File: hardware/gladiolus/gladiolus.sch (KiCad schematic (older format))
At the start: 133 parts, among them J1 NEIGHBOR1, J2 NEIGHBOR2, J7 BONUS_ROW, P1 CONN_01X05, Q1 Q_NPN_BEC, U1 THS4520RGT, U2 AD8330ARQZ, U3 AD9283, U4 AD9704, U5 LMH6643

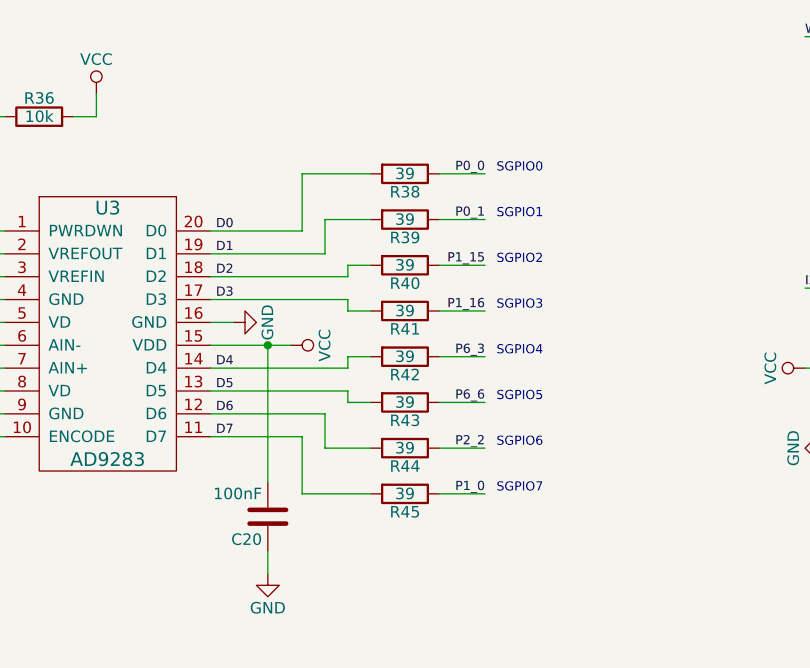
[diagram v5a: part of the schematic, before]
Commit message: Gladiolus: updated series resistor values to match those used at ShmooCon 2017
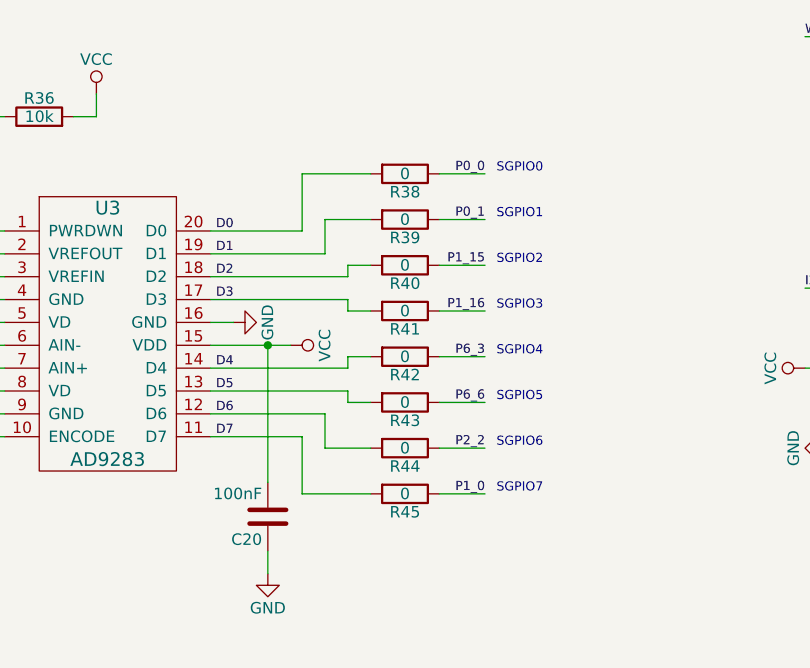
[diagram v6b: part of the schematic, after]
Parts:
- R38, R39, R40, R41, R42, R43, R44, R45: value 39 -> 0; Description RES SMD 39 OHM 5% 1/10W 0603 -> RES SMD 0.0OHM JUMPER 1/10W 0603; Part Number RC0603JR-0739RL -> RC0603JR-070RL

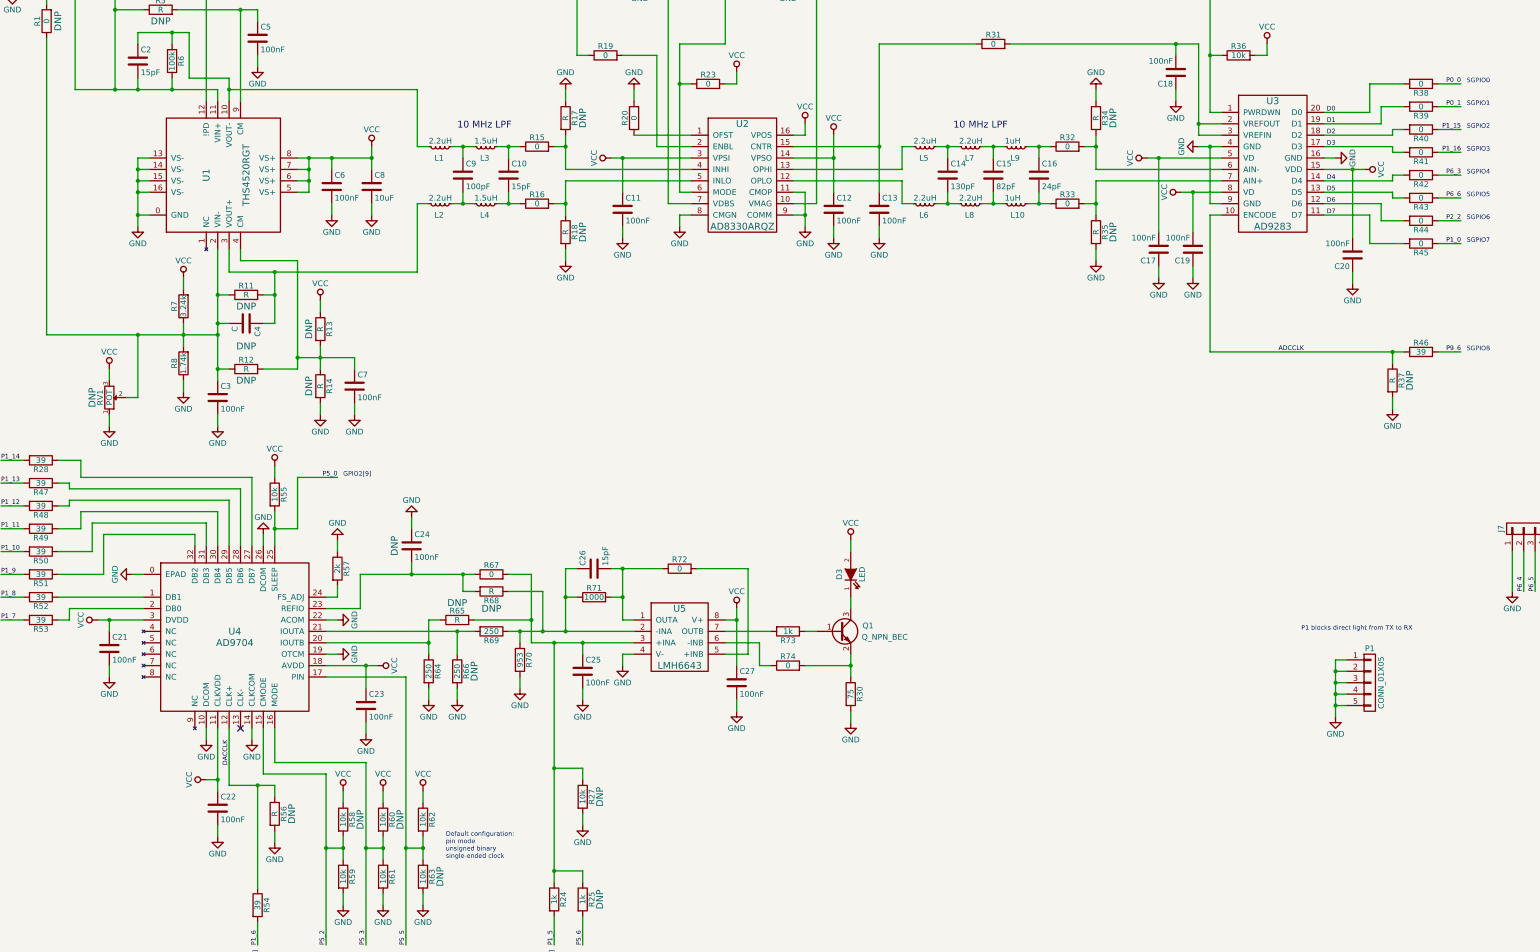
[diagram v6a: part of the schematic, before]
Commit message: Gladiolus: added LED/photodiode expansion to P1
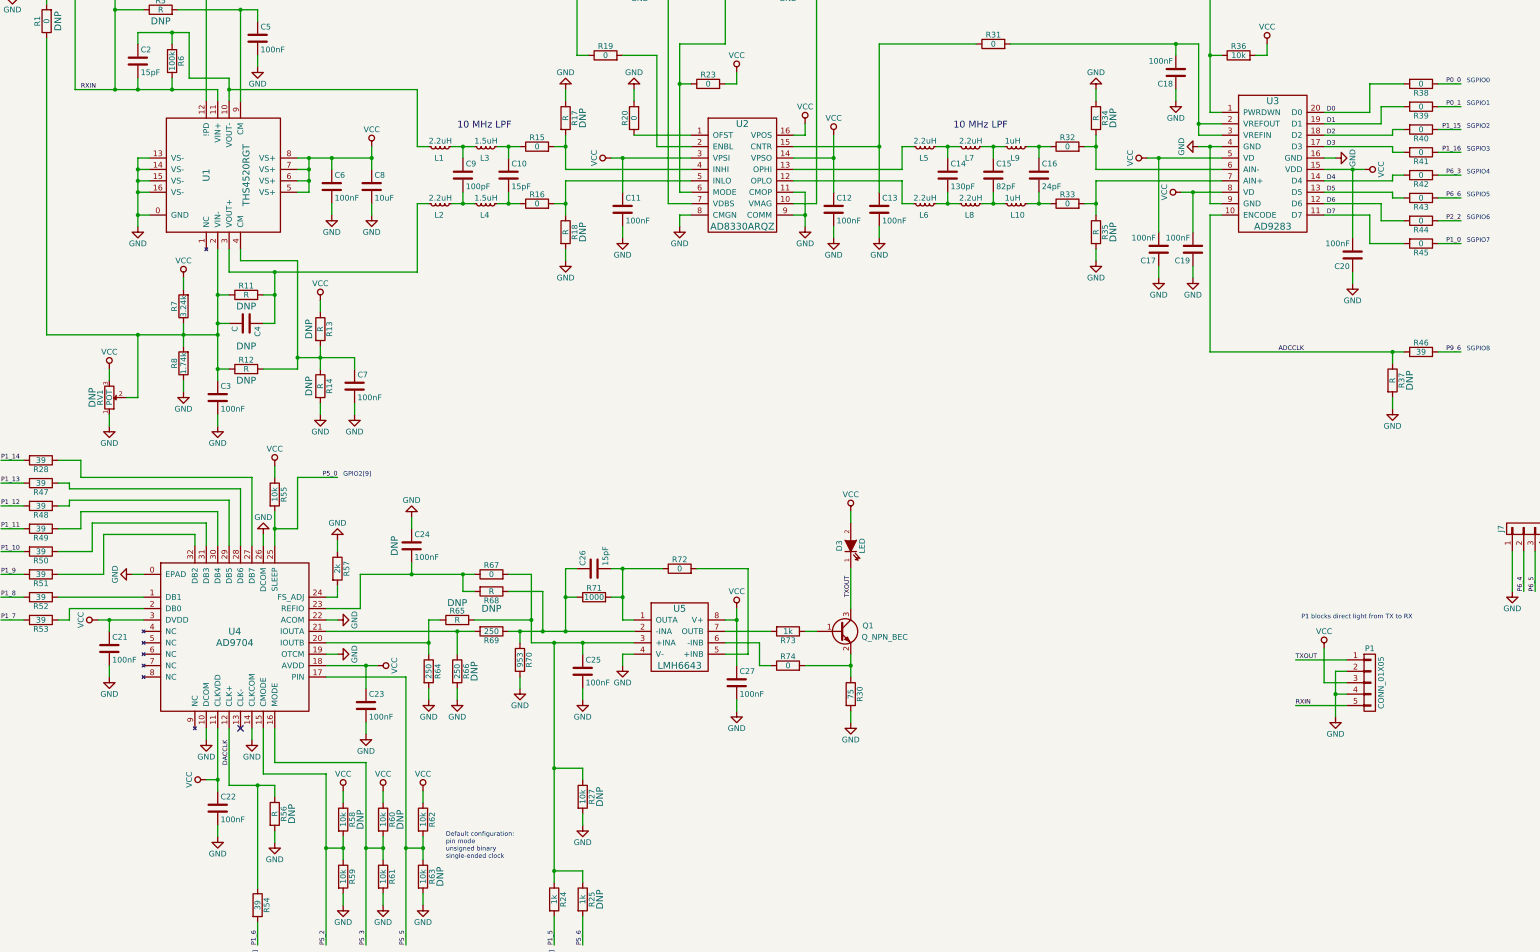
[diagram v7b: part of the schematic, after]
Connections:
- net GND: no longer P1.1 (P1), P1.3 (P3), P1.5 (P5)
- net VCC: now also P1.3 (P3)
- net RXIN: now reaches C2.2, D1.2 (A), D2.2 (A), R5.1, R6.2, U1.11 (VIN+)
- net RXIN: now also P1.5 (P5)
- net TXOUT: now reaches D3.1 (K), Q1.3 (C)
- net TXOUT: now also P1.1 (P1)
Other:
- moved on the sheet: D3
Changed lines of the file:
@@
 L LED D3
 U 1 1 58496E3C
-P 8450 6900
-F 0 "D3" H 8450 7000 50  0000 C CNN
-F 1 "LED" H 8450 6800 50  0000 C CNN
-F 2 "LEDs:LED-5MM" H 8450 6900 50  0001 C CNN
-F 3 "" H 8450 6900 50  0000 C CNN
-F 4 "Vishay" H 8450 6900 60  0001 C CNN "Manufacturer"
-F 5 "TSHF5210" H 8450 6900 60  0001 C CNN "Part Number"
-F 6 "Infrared (IR) Emitter 890nm 1.4V 100mA 120mW/sr @ 100mA 20° Radial, 5mm Dia (T 1 3/4)" H 8450 6900 60  0001 C CNN "Description"
-	1    8450 6900
+P 8450 6650
+F 0 "D3" H 8450 6750 50  0000 C CNN
+F 1 "LED" H 8450 6550 50  0000 C CNN
+F 2 "LEDs:LED-5MM" H 8450 6650 50  0001 C CNN
+F 3 "" H 8450 6650 50  0000 C CNN
+F 4 "Vishay" H 8450 6650 60  0001 C CNN "Manufacturer"
+F 5 "TSHF5210" H 8450 6650 60  0001 C CNN "Part Number"
+F 6 "Infrared (IR) Emitter 890nm 1.4V 100mA 120mW/sr @ 100mA 20° Radial, 5mm Dia (T 1 3/4)" H 8450 6650 60  0001 C CNN "Description"
+	1    8450 6650
 	0    -1   -1   0
 $EndComp
@@
 L VCC #PWR046
 U 1 1 58498676
-P 8450 6600
-F 0 "#PWR046" H 8450 6450 50  0001 C CNN
-F 1 "VCC" H 8450 6750 50  0000 C CNN
-F 2 "" H 8450 6600 60  0000 C CNN
-F 3 "" H 8450 6600 60  0000 C CNN
-	1    8450 6600
+P 8450 6350
+F 0 "#PWR046" H 8450 6200 50  0001 C CNN
+F 1 "VCC" H 8450 6500 50  0000 C CNN
+F 2 "" H 8450 6350 60  0000 C CNN
+F 3 "" H 8450 6350 60  0000 C CNN
+	1    8450 6350
 	1    0    0    -1
 $EndComp
@@
 	1    0    0    -1
 $EndComp
-Text Notes 12400 7400 0    40   ~ 0
+Text Notes 12400 7300 0    40   ~ 0
 P1 blocks direct light from TX to RX
 $Comp
@@
 Wire Wire Line
 	5550 7800 5550 7900
-Connection ~ 12700 8050
-Wire Wire Line
-	12700 8050 12800 8050
-Connection ~ 12700 7950
-Wire Wire Line
-	12700 7950 12800 7950
-Connection ~ 12700 7850
-Wire Wire Line
-	12700 7850 12800 7850
-Connection ~ 12700 7750
-Wire Wire Line
-	12800 7750 12700 7750
-Wire Wire Line
-	12700 7650 12700 8150
-Wire Wire Line
-	12800 7650 12700 7650
+Wire Wire Line
+	12350 8050 12800 8050
+Wire Wire Line
+	12800 7650 12350 7650
 Wire Wire Line
 	11600 3750 11600 4950
@@
 	8050 7400 8150 7400
 Wire Wire Line
-	8450 7100 8450 7200
+	8450 6850 8450 7200
 Wire Wire Line
 	8450 7600 8450 7800
@@
 	8450 8100 8450 8200
 Wire Wire Line
-	8450 6600 8450 6700
+	8450 6350 8450 6450
 Wire Wire Line
 	13000 2600 13300 2600
@@
 	6100 9600 6100 9500
 Wire Wire Line
-	6100 9500 5850 9500
+	5850 9500 6100 9500
 Connection ~ 5850 9500
 $Comp
@@
 Wire Wire Line
 	6600 800  6600 900
+Text Label 1700 2650 0    40   ~ 0
+RXIN
+Text Label 12350 8050 0    40   ~ 0
+RXIN
+Text Label 12350 7650 0    40   ~ 0
+TXOUT
+Text Label 8450 7100 1    40   ~ 0
+TXOUT
+Wire Wire Line
+	12800 7750 12700 7750
+Wire Wire Line
+	12700 7750 12700 8150
+Wire Wire Line
+	12800 7950 12700 7950
+Connection ~ 12700 7950
+$Comp
+L VCC #PWR?
+U 1 1 5883D349
+P 12600 7550
+F 0 "#PWR?" H 12600 7400 50  0001 C CNN
+F 1 "VCC" H 12600 7700 50  0000 C CNN
+F 2 "" H 12600 7550 60  0000 C CNN
+F 3 "" H 12600 7550 60  0000 C CNN
+	1    12600 7550
+	1    0    0    -1
+$EndComp
+Wire Wire Line
+	12800 7850 12600 7850
+Wire Wire Line
+	12600 7850 12600 7550
 $EndSCHEMATC

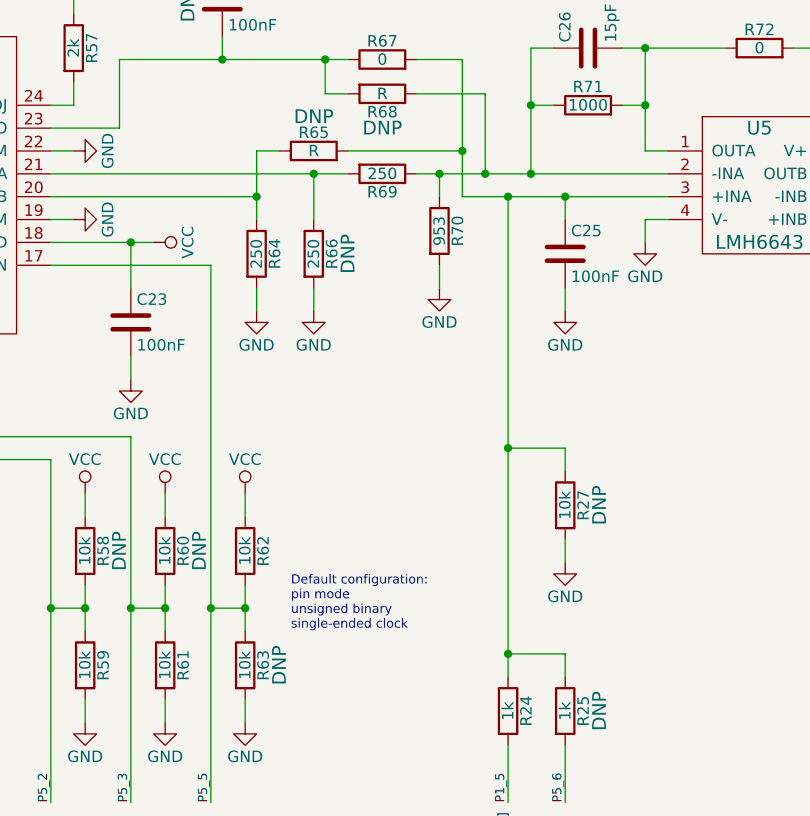
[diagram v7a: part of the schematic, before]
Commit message: Added part numbers for R57, R64, R66, R69, & R71; Changed values of R64, R66, & R69 to reflect part.
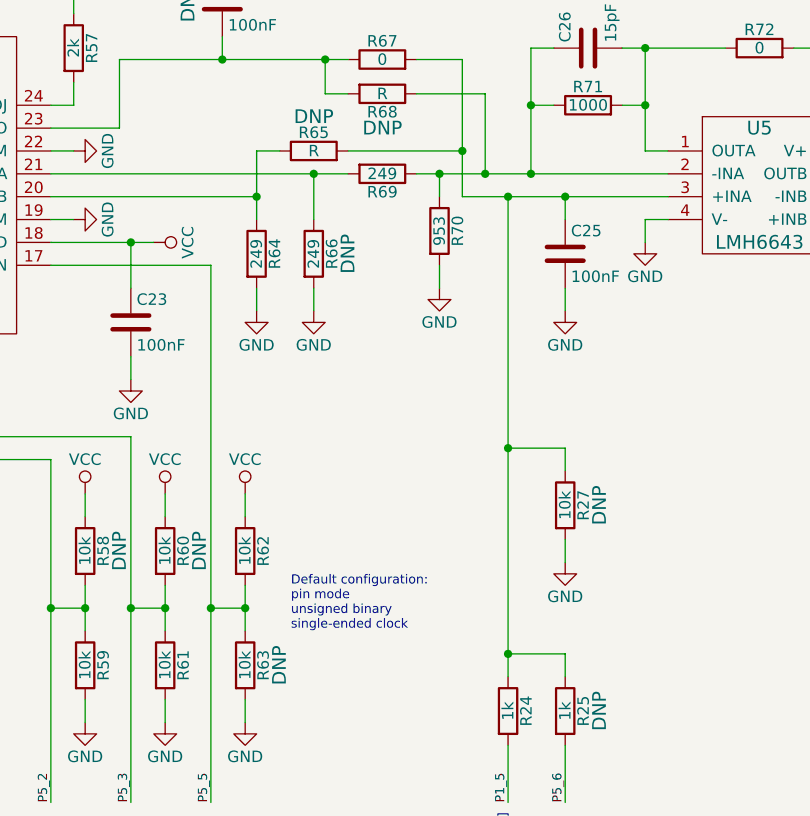
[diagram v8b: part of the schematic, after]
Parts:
- R57: Description (none) -> RES SMD 2K OHM 5% 1/10W 0603; Manufacturer (none) -> Yageo; Part Number (none) -> 311-2.0KGR
- R64, R66, R69: value 250 -> 249; Description (none) -> RES SMD 249 OHM 1% 1/10W 0603; Manufacturer (none) -> Yageo; Part Number (none) -> 311-249HR
- R71: Description (none) -> RES SMD 1K OHM 5% 1/10W 0603; Manufacturer (none) -> Yageo; Part Number (none) -> 311-1.0KGR
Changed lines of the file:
@@
 F 2 "gsg-modules:0603" V 6130 7100 50  0001 C CNN
 F 3 "" H 6200 7100 50  0000 C CNN
+F 4 "Yageo" H 6200 7100 60  0001 C CNN "Manufacturer"
+F 5 "311-1.0KGR" H 6200 7100 60  0001 C CNN "Part Number"
+F 6 "RES SMD 1K OHM 5% 1/10W 0603" H 6200 7100 60  0001 C CNN "Description"
 	1    6200 7100
 	0    -1   -1   0
@@
 P 4750 7750
 F 0 "R64" V 4830 7750 50  0000 C CNN
-F 1 "250" V 4750 7750 50  0000 C CNN
+F 1 "249" V 4750 7750 50  0000 C CNN
 F 2 "gsg-modules:0603" V 4680 7750 50  0001 C CNN
 F 3 "" H 4750 7750 50  0000 C CNN
+F 4 "Yageo" H 4750 7750 60  0001 C CNN "Manufacturer"
+F 5 "311-249HR" H 4750 7750 60  0001 C CNN "Part Number"
+F 6 "RES SMD 249 OHM 1% 1/10W 0603" H 4750 7750 60  0001 C CNN "Description"
 	1    4750 7750
 	1    0    0    -1
@@
 F 2 "gsg-modules:0603" V 3880 6850 50  0001 C CNN
 F 3 "" H 3950 6850 50  0000 C CNN
+F 4 "Yageo" H 3950 6850 60  0001 C CNN "Manufacturer"
+F 5 "311-2.0KGR" H 3950 6850 60  0001 C CNN "Part Number"
+F 6 "RES SMD 2K OHM 5% 1/10W 0603" H 3950 6850 60  0001 C CNN "Description"
 	1    3950 6850
 	1    0    0    -1
@@
 P 5300 7400
 F 0 "R69" V 5380 7400 50  0000 C CNN
-F 1 "250" V 5300 7400 50  0000 C CNN
+F 1 "249" V 5300 7400 50  0000 C CNN
 F 2 "gsg-modules:0603" V 5230 7400 50  0001 C CNN
 F 3 "" H 5300 7400 50  0000 C CNN
+F 4 "Yageo" H 5300 7400 60  0001 C CNN "Manufacturer"
+F 5 "311-249HR" H 5300 7400 60  0001 C CNN "Part Number"
+F 6 "RES SMD 249 OHM 1% 1/10W 0603" H 5300 7400 60  0001 C CNN "Description"
 	1    5300 7400
 	0    1    1    0
@@
 P 5000 7750
 F 0 "R66" V 5080 7750 50  0000 C CNN
-F 1 "250" V 5000 7750 50  0000 C CNN
+F 1 "249" V 5000 7750 50  0000 C CNN
 F 2 "gsg-modules:0603" V 4930 7750 50  0001 C CNN
 F 3 "" H 5000 7750 50  0000 C CNN
-F 4 "DNP" V 5150 7750 60  0000 C CNN "Note"
+F 4 "Yageo" H 5000 7750 60  0001 C CNN "Manufacturer"
+F 5 "311-249HR" H 5000 7750 60  0001 C CNN "Part Number"
+F 6 "RES SMD 249 OHM 1% 1/10W 0603" H 5000 7750 60  0001 C CNN "Description"
+F 7 "DNP" V 5150 7750 60  0000 C CNN "Note"
 	1    5000 7750
 	1    0    0    -1
@@
 	6100 9600 6100 9500
 Wire Wire Line
-	5850 9500 6100 9500
+	6100 9500 5850 9500
 Connection ~ 5850 9500
 $Comp
@@
 Connection ~ 12700 7950
 $Comp
-L VCC #PWR?
+L VCC #PWR090
 U 1 1 5883D349
 P 12600 7550
-F 0 "#PWR?" H 12600 7400 50  0001 C CNN
+F 0 "#PWR090" H 12600 7400 50  0001 C CNN
 F 1 "VCC" H 12600 7700 50  0000 C CNN
 F 2 "" H 12600 7550 60  0000 C CNN
